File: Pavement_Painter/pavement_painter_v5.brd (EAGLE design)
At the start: 63 x 99.3 mm, 60 parts, among them J3 POWER_JACK, Q1 TIP120, Q10 TIP120, Q11 TIP120, Q12 TIP120, Q13 TIP120, Q14 TIP120, Q15 TIP120, Q16 TIP120, Q2 TIP120, Q3 TIP120, Q4 TIP120, Q5 TIP120, Q6 TIP120, Q7 TIP120, Q8 TIP120, Q9 TIP120

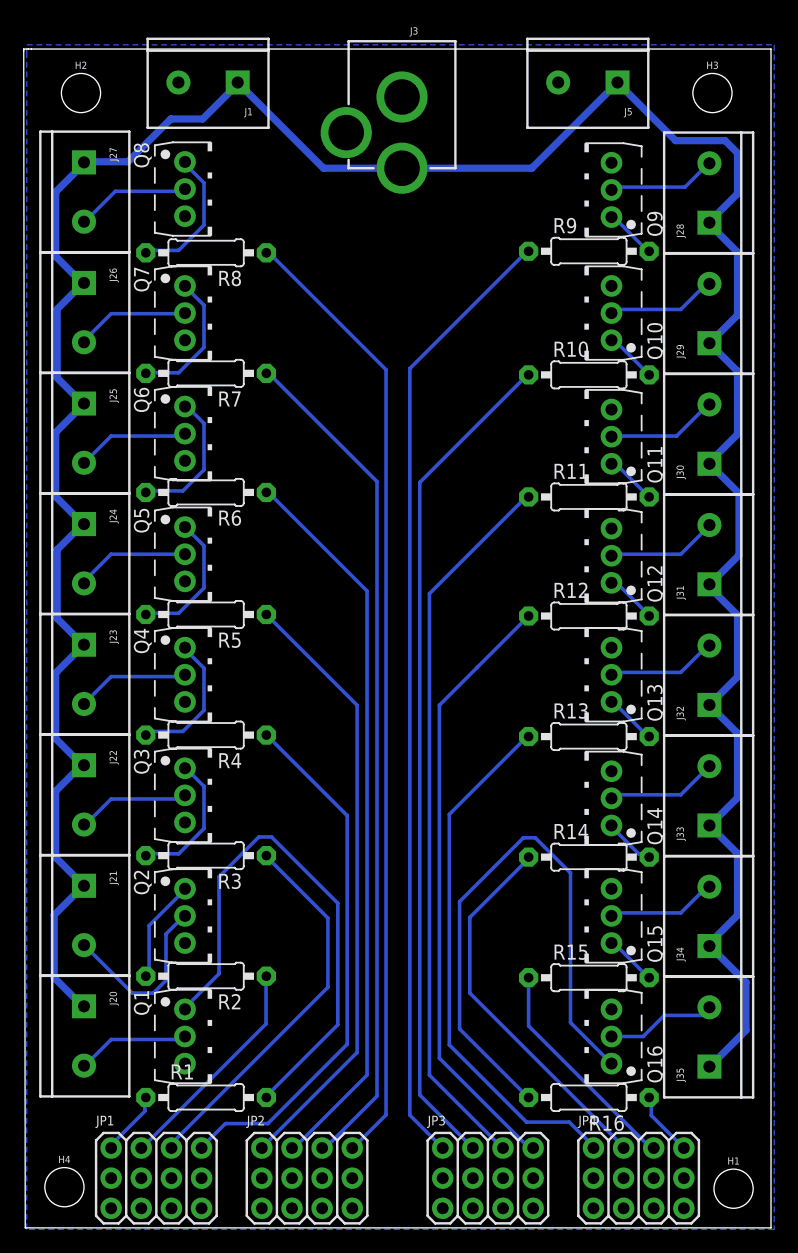
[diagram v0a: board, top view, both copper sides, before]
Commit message: Updating jumper numbers, slight changes to layout
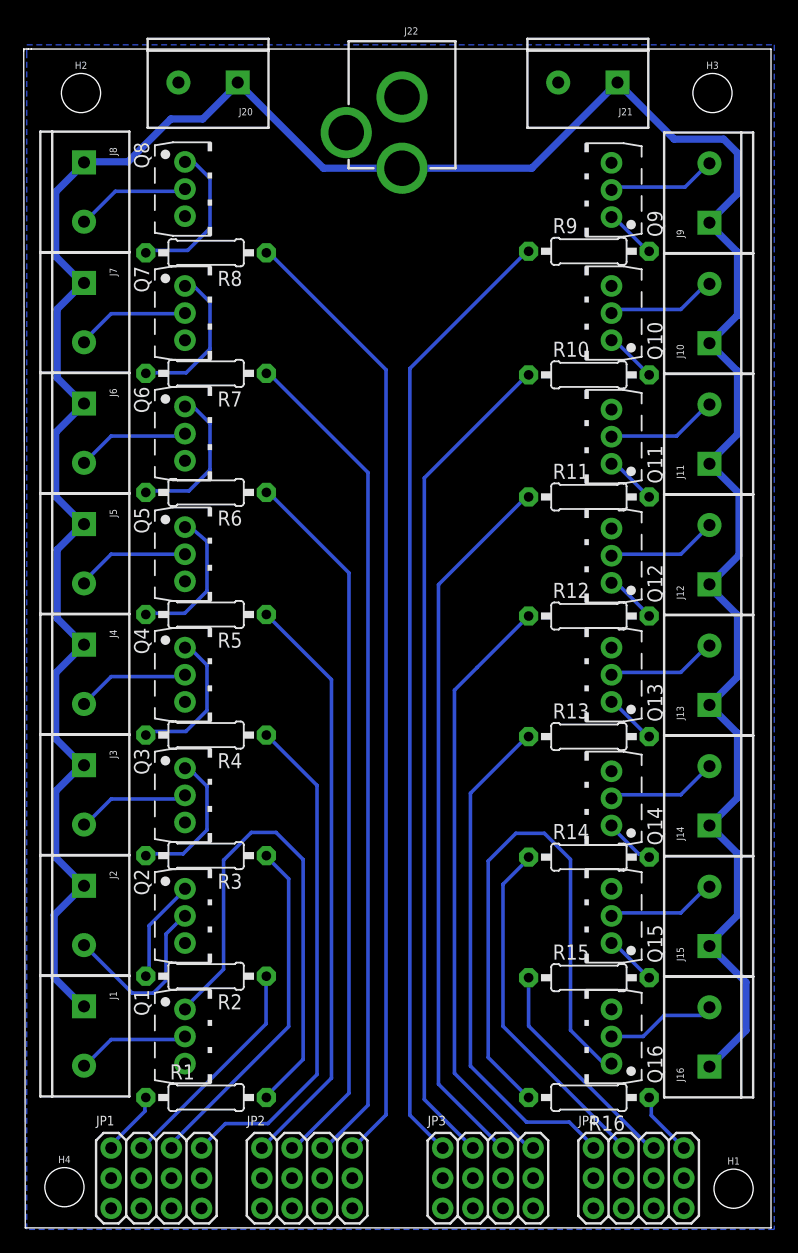
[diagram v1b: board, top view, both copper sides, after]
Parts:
- removed J24: (no value), SparkFun-Connectors:SCREWTERMINAL-5MM-2-400MIL
- added J2: (no value), SparkFun-Connectors:SCREWTERMINAL-5MM-2-400MIL
- J22: value (none) -> POWER_JACK; device SparkFun-Connectors:SCREWTERMINAL-5MM-2-400MIL -> SparkFun-Connectors:POWER_JACK_PTH
- J3: value POWER_JACK -> (none); device SparkFun-Connectors:POWER_JACK_PTH -> SparkFun-Connectors:SCREWTERMINAL-5MM-2-400MIL
- moved J21 81.8 mm to (50.0, 96.9), turned to 180 degrees
- moved J1 79.4 mm to (4.70, 18.7), turned to 270 degrees
- moved J20 79.4 mm to (18.0, 96.9), turned to 180 degrees
- moved J22 69.5 mm to (31.9, 103.0), turned to 180 degrees
- moved J3 69.5 mm to (4.70, 39.0), turned to 270 degrees
- moved J5 58.9 mm to (4.70, 59.3), turned to 270 degrees
- renumbered J23 to J4, J25 to J6, J26 to J7, J27 to J8, J28 to J9, J29 to J10, J30 to J11, J31 to J12, J32 to J13, J33 to J14, J34 to J15, J35 to J16
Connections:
- net +12V: now also J2.1, J22.PWR, J3.1; no longer J22.1, J24.1, J3.PWR
- net GND: now also J20.2, J21.2, J22.GND, J22.GNDBREAK; no longer J1.2, J3.GND, J3.GNDBREAK, J5.2
- net N$1: now also J2.2; no longer J21.2
- net N$3: now also J1.2; no longer J20.2
- net N$5: now also J3.2; no longer J22.2
- net N$9: now also J5.2; no longer J24.2
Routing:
- net PCA_SOL3: track 32.3 -> 29.6 mm
- net PCA_SOL14: track 31.9 -> 29.6 mm
- net PCA_SOL4: track 44.8 -> 42.7 mm
- net PCA_SOL5: track 51.4 -> 49.7 mm
- net PCA_SOL13: track 44.6 -> 43.2 mm
- net N$16: track 11.8 -> 13.1 mm
- net PCA_SOL6: track 61.6 -> 60.3 mm
- net N$14: track 11.6 -> 12.9 mm
- net N$4: track 44.9 -> 43.8 mm
- net PCA_SOL12: track 51.4 -> 50.4 mm
- net N$12: track 11.8 -> 12.8 mm
- net N$10: track 11.6 -> 12.4 mm
- net PCA_SOL7: track 71.3 -> 70.7 mm
- net PCA_SOL11: track 61.0 -> 60.4 mm
- net N$8: track 11.7 -> 12.3 mm
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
